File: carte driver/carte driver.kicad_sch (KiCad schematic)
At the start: 38 parts, among them J1 UART CP, J10 STEPPER 4, J11 STEPPER 3, J2 Conn_01x03, J3 UART BONUS, J6 STEPPER G, J7 STEPPER D, J8 STEPPER 1, J9 STEPPER 2, SW2 SW_DIP_x02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

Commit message: c'est l'heure de dodo j'ai bien taffé
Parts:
- added D2: LED_Small, LED_SMD:LED_1206_3216Metric, symbol Device:LED_Small
- added J4: Conn_01x02, Connector_Molex:Molex_KK-254_AE-6410-02A_1x02_P2.54mm_Vertical, symbol Connector_Generic:Conn_01x02
- added R1, R2, R5: 1k, Resistor_SMD:R_1206_3216Metric_Pad1.30x1.75mm_HandSolder, symbol Device:R_Small
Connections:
- net +24V: now also J2.2 (Pin_2); no longer J2.1 (Pin_1)
- net +3.3V: now also J2.1 (Pin_1); no longer U10.12 (VCC_3V3)
- net +5V: now also J4.1 (Pin_1), R5.1; no longer J2.2 (Pin_2)
- net DIR 1: now also U10.4 (GPIO4_D3/A3); no longer U10.2 (GPIO2_D1/A1)
- net DIR 2: now also U10.6 (GPIO6_D5/A5/I2C_SCL); no longer U10.4 (GPIO4_D3/A3)
- net DIR 3: now also U10.2 (GPIO2_D1/A1); no longer U10.6 (GPIO6_D5/A5/I2C_SCL)
- net DIR 5: now also U10.15 (GPIO38_DVP_VSYNC/I2S_SD); no longer U10.16 (GPIO39_CAM_SCL/I2S_SCK)
- net GND: now also D2.1 (K), J4.2 (Pin_2)
- net RX B: now also R1.2; no longer U10.18 (GPIO41_PDM_DATA/RX1)
- net STEP 1: now also U10.3 (GPIO3_D2/A2); no longer U10.1 (GPIO1_D0/A0)
- net STEP 2: now also U10.5 (GPIO5_D4/A4/I2C_SDA); no longer U10.3 (GPIO3_D2/A2)
- net STEP 3: now also U10.1 (GPIO1_D0/A0); no longer U10.5 (GPIO5_D4/A4/I2C_SDA)
- net STEP 5: now also U10.16 (GPIO39_CAM_SCL/I2S_SCK); no longer U10.15 (GPIO38_DVP_VSYNC/I2S_SD)
- net TX B: now also R2.2; no longer U10.19 (GPIO42_PDM_CLK/TX1)
- net at U10.20 (GPIO10_XMCLK/ADC_BAT): now also R2.1
- new net: D2.2 (A), R5.2
- new net: R1.1, U10.19 (GPIO42_PDM_CLK/TX1)
- no-connect marks 30 -> 31

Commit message: apdavph
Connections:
- net at U3.3 (M1B): now also J8.1 (Pin_1); no longer J8.3 (Pin_3)
- net at U3.4 (M1A): now also J8.2 (Pin_2); no longer J8.1 (Pin_1)
- net at U3.5 (M2A): now also J8.3 (Pin_3); no longer J8.2 (Pin_2)
- net at U6.3 (M1B): now also J10.1 (Pin_1); no longer J10.3 (Pin_3)
- net at U6.4 (M1A): now also J10.2 (Pin_2); no longer J10.1 (Pin_1)
- net at U6.5 (M2A): now also J10.3 (Pin_3); no longer J10.2 (Pin_2)
- net at J9.1 (Pin_1): now also U4.3 (M1B); no longer U4.4 (M1A)
- net at J9.2 (Pin_2): now also U4.4 (M1A); no longer U4.5 (M2A)
- net at J9.3 (Pin_3): now also U4.5 (M2A); no longer U4.3 (M1B)
- net at J7.1 (Pin_1): now also U2.3 (M1B); no longer U2.4 (M1A)
- net at J7.2 (Pin_2): now also U2.4 (M1A); no longer U2.5 (M2A)
- net at J7.3 (Pin_3): now also U2.5 (M2A); no longer U2.3 (M1B)
- net at U1.3 (M1B): now also J6.1 (Pin_1); no longer J6.3 (Pin_3)
- net at U1.4 (M1A): now also J6.2 (Pin_2); no longer J6.1 (Pin_1)
- net at U1.5 (M2A): now also J6.3 (Pin_3); no longer J6.2 (Pin_2)
- net at J11.1 (Pin_1): now also U5.3 (M1B); no longer U5.4 (M1A)
- net at J11.2 (Pin_2): now also U5.4 (M1A); no longer U5.5 (M2A)
- net at J11.3 (Pin_3): now also U5.5 (M2A); no longer U5.3 (M1B)
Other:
- moved on the sheet: J10, J11, J6, J7, J8, J9

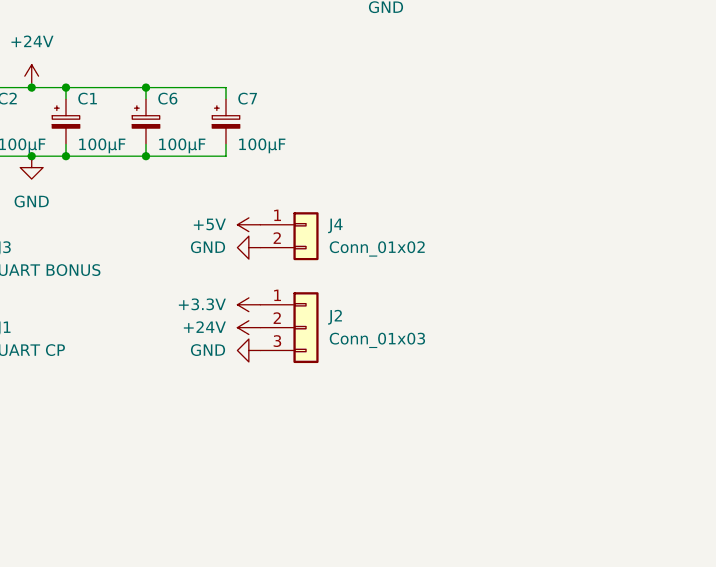
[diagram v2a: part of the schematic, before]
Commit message: changes power input and draw modif
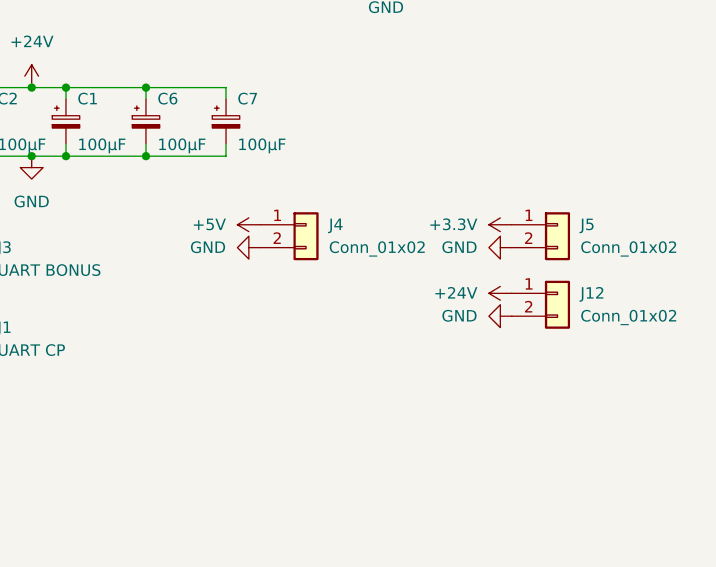
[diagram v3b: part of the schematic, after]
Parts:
- removed J2: Conn_01x03, Connector_JST:JST_EH_B3B-EH-A_1x03_P2.50mm_Vertical, symbol Connector_Generic:Conn_01x03
- added J12: Conn_01x02, Connector_AMASS:AMASS_XT60-F_1x02_P7.20mm_Vertical, symbol Connector_Generic:Conn_01x02
- added J5: Conn_01x02, Connector_AMASS:AMASS_XT30U-F_1x02_P5.0mm_Vertical, symbol Connector_Generic:Conn_01x02
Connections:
- net +24V: now also J12.1 (Pin_1)
- net +3.3V: now also J5.1 (Pin_1)
- net GND: now also J12.2 (Pin_2), J5.2 (Pin_2)
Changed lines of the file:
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@@
 	(symbol
 		(lib_id "power:+3.3V")
-		(at 212.09 151.13 90)
+		(at 240.03 142.24 90)
 		(unit 1)
 		(exclude_from_sim no)
@@
 		(fields_autoplaced yes)
 		(property "Reference" "#PWR015"
-			(at 215.9 151.13 0)
+			(at 243.84 142.24 0)
 			(effects
 				(font
@@
 		)
 		(property "Value" "+3.3V"
-			(at 208.28 151.1299 90)
+			(at 236.22 142.2399 90)
 			(effects
 				(font
@@
 		)
 		(property "Footprint" ""
-			(at 212.09 151.13 0)
+			(at 240.03 142.24 0)
 			(effects
 				(font
@@
 		)
 		(property "Datasheet" ""
-			(at 212.09 151.13 0)
+			(at 240.03 142.24 0)
 			(effects
 				(font
@@
 		)
 		(property "Description" "Power symbol creates a global label with name \"+3.3V\""
-			(at 212.09 151.13 0)
+			(at 240.03 142.24 0)
 			(effects
 				(font
@@
 	(symbol
 		(lib_id "power:GND")
-		(at 212.09 156.21 270)
+		(at 240.03 144.78 270)
 		(unit 1)
 		(exclude_from_sim no)
@@
 		(fields_autoplaced yes)
 		(property "Reference" "#PWR04"
-			(at 205.74 156.21 0)
+			(at 233.68 144.78 0)
 			(effects
 				(font
@@
 		)
 		(property "Value" "GND"
-			(at 208.28 156.2099 90)
+			(at 236.22 144.7799 90)
 			(effects
 				(font
@@
 		)
 		(property "Footprint" ""
-			(at 212.09 156.21 0)
+			(at 240.03 144.78 0)
 			(effects
 				(font
@@
 		)
 		(property "Datasheet" ""
-			(at 212.09 156.21 0)
+			(at 240.03 144.78 0)
 			(effects
 				(font
@@
 		)
 		(property "Description" "Power symbol creates a global label with name \"GND\" , ground"
-			(at 212.09 156.21 0)
+			(at 240.03 144.78 0)
 			(effects
 				(font
@@
 	)
 	(symbol
+		(lib_id "power:GND")
+		(at 240.03 152.4 270)
+		(unit 1)
+		(exclude_from_sim no)
+		(in_bom yes)
+		(on_board yes)
+		(dnp no)
+		(fields_autoplaced yes)
+		(property "Reference" "#PWR08"
+			(at 233.68 152.4 0)
+			(effects
+				(font
+					(size 1.27 1.27)
+				)
+				(hide yes)
+			)
+		)
+		(property "Value" "GND"
+			(at 236.22 152.3999 90)
+			(effects
+				(font
+					(size 1.27 1.27)
+				)
+				(justify right)
+			)
+		)
+		(property "Footprint" ""
+			(at 240.03 152.4 0)
+			(effects
+				(font
+					(size 1.27 1.27)
+				)
+				(hide yes)
+			)
+		)
+		(property "Datasheet" ""
+			(at 240.03 152.4 0)
+			(effects
+				(font
+					(size 1.27 1.27)
+				)
+				(hide yes)
+			)
+		)
+		(property "Description" "Power symbol creates a global label with name \"GND\" , ground"
+			(at 240.03 152.4 0)
+			(effects
+				(font
+					(size 1.27 1.27)
+				)
+				(hide yes)
+			)
+		)
+		(pin "1"
+		)
+		(instances
+			(project "carte driver"
+				(path "/78588076-997a-4987-8ae5-538bbbdafc63"
+					(reference "#PWR08")
+					(unit 1)
+				)
+			)
+		)
+	)
+	(symbol
 		(lib_id "Device:R_Small")
 		(at 140.97 144.78 0)
@@
 	(symbol
 		(lib_id "power:+24V")
-		(at 212.09 153.67 90)
+		(at 240.03 149.86 90)
 		(unit 1)
 		(exclude_from_sim no)
@@
 		(fields_autoplaced yes)
 		(property "Reference" "#PWR01"
-			(at 215.9 153.67 0)
+			(at 243.84 149.86 0)
 			(effects
 				(font
@@
 		)
 		(property "Value" "+24V"
-			(at 208.28 153.6699 90)
+			(at 236.22 149.8599 90)
 			(effects
 				(font
@@
 		)
 		(property "Footprint" ""
-			(at 212.09 153.67 0)
+			(at 240.03 149.86 0)
 			(effects
 				(font
@@
 		)
 		(property "Datasheet" ""
-			(at 212.09 153.67 0)
+			(at 240.03 149.86 0)
 			(effects
 				(font
@@
 		)
 		(property "Description" "Power symbol creates a global label with name \"+24V\""
-			(at 212.09 153.67 0)
+			(at 240.03 149.86 0)
 			(effects
 				(font
@@
 	)
 	(symbol
+		(lib_id "Connector_Generic:Conn_01x02")
+		(at 245.11 149.86 0)
+		(unit 1)
+		(exclude_from_sim no)
+		(in_bom yes)
+		(on_board yes)
+		(dnp no)
+		(fields_autoplaced yes)
+		(property "Reference" "J12"
+			(at 247.65 149.8599 0)
+			(effects
+				(font
+					(size 1.27 1.27)
+				)
+				(justify left)
+			)
+		)
+		(property "Value" "Conn_01x02"
+			(at 247.65 152.3999 0)
+			(effects
+				(font
+					(size 1.27 1.27)
+				)
+				(justify left)
+			)
+		)
+		(property "Footprint" "Connector_AMASS:AMASS_XT60-F_1x02_P7.20mm_Vertical"
+			(at 245.11 149.86 0)
+			(effects
+				(font
+					(size 1.27 1.27)
+				)
+				(hide yes)
+			)
+		)
+		(property "Datasheet" "~"
+			(at 245.11 149.86 0)
+			(effects
+				(font
+					(size 1.27 1.27)
+				)
+				(hide yes)
+			)
+		)
+		(property "Description" "Generic connector, single row, 01x02, script generated (kicad-library-utils/schlib/autogen/connector/)"
+			(at 245.11 149.86 0)
+			(effects
+				(font
+					(size 1.27 1.27)
+				)
+				(hide yes)
+			)
+		)
+		(pin "1"
+		)
+		(pin "2"
+		)
+		(instances
+			(project "carte driver"
+				(path "/78588076-997a-4987-8ae5-538bbbdafc63"
+					(reference "J12")
+					(unit 1)
+				)
+			)
+		)
+	)
+	(symbol
 		(lib_id "Switch:SW_DIP_x02")
 		(at 106.68 48.26 0)
@@
 	)
 	(symbol
+		(lib_id "Connector_Generic:Conn_01x02")
+		(at 245.11 142.24 0)
+		(unit 1)
+		(exclude_from_sim no)
+		(in_bom yes)
+		(on_board yes)
+		(dnp no)
+		(fields_autoplaced yes)
+		(property "Reference" "J5"
+			(at 247.65 142.2399 0)
+			(effects
+				(font
+					(size 1.27 1.27)
+				)
+				(justify left)
+			)
+		)
+		(property "Value" "Conn_01x02"
+			(at 247.65 144.7799 0)
+			(effects
+				(font
+					(size 1.27 1.27)
+				)
+				(justify left)
+			)
+		)
+		(property "Footprint" "Connector_AMASS:AMASS_XT30U-F_1x02_P5.0mm_Vertical"
+			(at 245.11 142.24 0)
+			(effects
+				(font
+					(size 1.27 1.27)
+				)
+				(hide yes)
+			)
+		)
+		(property "Datasheet" "~"
+			(at 245.11 142.24 0)
+			(effects
+				(font
+					(size 1.27 1.27)
+				)
+				(hide yes)
+			)
+		)
+		(property "Description" "Generic connector, single row, 01x02, script generated (kicad-library-utils/schlib/autogen/connector/)"
+			(at 245.11 142.24 0)
+			(effects
+				(font
+					(size 1.27 1.27)
+				)
+				(hide yes)
+			)
+		)
+		(pin "1"
+		)
+		(pin "2"
+		)
+		(instances
+			(project "carte driver"
+				(path "/78588076-997a-4987-8ae5-538bbbdafc63"
+					(reference "J5")
+					(unit 1)
+				)
+			)
+		)
+	)
+	(symbol
 		(lib_id "power:+3.3V")
 		(at 175.26 97.79 0)
@@
 					(unit 1)
 				)
-			)
-		)
-	)
-	(symbol
-		(lib_id "Connector_Generic:Conn_01x03")
-		(at 217.17 153.67 0)
-		(unit 1)
-		(exclude_from_sim no)
-		(in_bom yes)
-		(on_board yes)
-		(dnp no)
-		(fields_autoplaced yes)
-		(property "Reference" "J2"
-			(at 219.71 152.3999 0)
-			(effects
-				(font
-					(size 1.27 1.27)
-				)
-				(justify left)
-			)
-		)
-		(property "Value" "Conn_01x03"
-			(at 219.71 154.9399 0)
-			(effects
-				(font
-					(size 1.27 1.27)
-				)
-				(justify left)
-			)
-		)
-		(property "Footprint" "Connector_JST:JST_EH_B3B-EH-A_1x03_P2.50mm_Vertical"
-			(at 217.17 153.67 0)
-			(effects
-				(font
-					(size 1.27 1.27)
-				)
-				(hide yes)
-			)
-		)
-		(property "Datasheet" "~"
-			(at 217.17 153.67 0)
-			(effects
-				(font
-					(size 1.27 1.27)
-				)
-				(hide yes)
-			)
-		)
-		(property "Description" "Generic connector, single row, 01x03, script generated (kicad-library-utils/schlib/autogen/connector/)"
-			(at 217.17 153.67 0)
-			(effects
-				(font
-					(size 1.27 1.27)
-				)
-				(hide yes)
-			)
-		)
-		(pin "2"
-		)
-		(pin "3"
-		)
-		(pin "1"
-		)
-		(instances
-			(project ""
-				(path "/78588076-997a-4987-8ae5-538bbbdafc63"
-					(reference "J2")
-					(unit 1)
-				)

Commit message: boh il y a des trucs à changé ducoup
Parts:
- J12: value Conn_01x02 -> conn 24v
- J4: value Conn_01x02 -> conn 5v
- J5: value Conn_01x02 -> conn 3.3v
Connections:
- net +24V: now also J12.2 (Pin_2); no longer J12.1 (Pin_1)
- net +3.3V: now also J5.2 (Pin_2); no longer J5.1 (Pin_1)
- net GND: now also J12.1 (Pin_1), J5.1 (Pin_1); no longer J12.2 (Pin_2), J5.2 (Pin_2)
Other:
- moved on the sheet: J12, J4, J5
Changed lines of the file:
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@@
 	(symbol
 		(lib_id "power:+3.3V")
-		(at 240.03 142.24 90)
+		(at 245.11 138.43 90)
 		(unit 1)
 		(exclude_from_sim no)
@@
 		(fields_autoplaced yes)
 		(property "Reference" "#PWR015"
-			(at 243.84 142.24 0)
+			(at 248.92 138.43 0)
 			(effects
 				(font
@@
 		)
 		(property "Value" "+3.3V"
-			(at 236.22 142.2399 90)
+			(at 241.3 138.4299 90)
 			(effects
 				(font
@@
 		)
 		(property "Footprint" ""
-			(at 240.03 142.24 0)
+			(at 245.11 138.43 0)
 			(effects
 				(font
@@
 		)
 		(property "Datasheet" ""
-			(at 240.03 142.24 0)
+			(at 245.11 138.43 0)
 			(effects
 				(font
@@
 		)
 		(property "Description" "Power symbol creates a global label with name \"+3.3V\""
-			(at 240.03 142.24 0)
+			(at 245.11 138.43 0)
 			(effects
 				(font
@@
 		)
 		(instances
-			(project ""
+			(project "carte driver"
 				(path "/78588076-997a-4987-8ae5-538bbbdafc63"
 					(reference "#PWR015")
@@
 	(symbol
 		(lib_id "power:GND")
-		(at 240.03 144.78 270)
+		(at 245.11 135.89 270)
 		(unit 1)
 		(exclude_from_sim no)
@@
 		(fields_autoplaced yes)
 		(property "Reference" "#PWR04"
-			(at 233.68 144.78 0)
+			(at 238.76 135.89 0)
 			(effects
 				(font
@@
 		)
 		(property "Value" "GND"
-			(at 236.22 144.7799 90)
+			(at 241.3 135.8899 90)
 			(effects
 				(font
@@
 		)
 		(property "Footprint" ""
-			(at 240.03 144.78 0)
+			(at 245.11 135.89 0)
 			(effects
 				(font
@@
 		)
 		(property "Datasheet" ""
-			(at 240.03 144.78 0)
+			(at 245.11 135.89 0)
 			(effects
 				(font
@@
 		)
 		(property "Description" "Power symbol creates a global label with name \"GND\" , ground"
-			(at 240.03 144.78 0)
+			(at 245.11 135.89 0)
 			(effects
 				(font
@@
 		)
 		(instances
-			(project ""
+			(project "carte driver"
 				(path "/78588076-997a-4987-8ae5-538bbbdafc63"
 					(reference "#PWR04")
@@
 	(symbol
 		(lib_id "power:GND")
-		(at 212.09 144.78 270)
+		(at 245.11 144.78 270)
 		(unit 1)
 		(exclude_from_sim no)
@@
 		(fields_autoplaced yes)
 		(property "Reference" "#PWR016"
-			(at 205.74 144.78 0)
+			(at 238.76 144.78 0)
 			(effects
 				(font
@@
 		)
 		(property "Value" "GND"
-			(at 208.28 144.7799 90)
+			(at 241.3 144.7799 90)
 			(effects
 				(font
@@
 		)
 		(property "Footprint" ""
-			(at 212.09 144.78 0)
+			(at 245.11 144.78 0)
 			(effects
 				(font
@@
 		)
 		(property "Datasheet" ""
-			(at 212.09 144.78 0)
+			(at 245.11 144.78 0)
 			(effects
 				(font
@@
 		)
 		(property "Description" "Power symbol creates a global label with name \"GND\" , ground"
-			(at 212.09 144.78 0)
+			(at 245.11 144.78 0)
 			(effects
 				(font
@@
 	(symbol
 		(lib_id "power:GND")
-		(at 240.03 152.4 270)
+		(at 245.11 148.59 270)
 		(unit 1)
 		(exclude_from_sim no)
@@
 		(fields_autoplaced yes)
 		(property "Reference" "#PWR08"
-			(at 233.68 152.4 0)
+			(at 238.76 148.59 0)
 			(effects
 				(font
@@
 		)
 		(property "Value" "GND"
-			(at 236.22 152.3999 90)
+			(at 241.3 148.5899 90)
 			(effects
 				(font
@@
 		)
 		(property "Footprint" ""
-			(at 240.03 152.4 0)
+			(at 245.11 148.59 0)
 			(effects
 				(font
@@
 		)
 		(property "Datasheet" ""
-			(at 240.03 152.4 0)
+			(at 245.11 148.59 0)
 			(effects
 				(font
@@
 		)
 		(property "Description" "Power symbol creates a global label with name \"GND\" , ground"
-			(at 240.03 152.4 0)
+			(at 245.11 148.59 0)
 			(effects
 				(font
@@
 	(symbol
 		(lib_id "power:+24V")
-		(at 240.03 149.86 90)
+		(at 245.11 151.13 90)
 		(unit 1)
 		(exclude_from_sim no)
@@
 		(fields_autoplaced yes)
 		(property "Reference" "#PWR01"
-			(at 243.84 149.86 0)
+			(at 248.92 151.13 0)
 			(effects
 				(font
@@
 		)
 		(property "Value" "+24V"
-			(at 236.22 149.8599 90)
+			(at 241.3 151.1299 90)
 			(effects
 				(font
@@
 		)
 		(property "Footprint" ""
-			(at 240.03 149.86 0)
+			(at 245.11 151.13 0)
 			(effects
 				(font
@@
 		)
 		(property "Datasheet" ""
-			(at 240.03 149.86 0)
+			(at 245.11 151.13 0)
 			(effects
 				(font
@@
 		)
 		(property "Description" "Power symbol creates a global label with name \"+24V\""
-			(at 240.03 149.86 0)
+			(at 245.11 151.13 0)
 			(effects
 				(font
@@
 	(symbol
 		(lib_id "Connector_Generic:Conn_01x02")
-		(at 217.17 142.24 0)
+		(at 250.19 142.24 0)
 		(unit 1)
 		(exclude_from_sim no)
@@
 		(fields_autoplaced yes)
 		(property "Reference" "J4"
-			(at 219.71 142.2399 0)
+			(at 252.73 142.2399 0)
 			(effects
 				(font
@@
 			)
 		)
-		(property "Value" "Conn_01x02"
-			(at 219.71 144.7799 0)
+		(property "Value" "conn 5v"
+			(at 252.73 144.7799 0)
 			(effects
 				(font
@@
 		)
 		(property "Footprint" "Connector_Molex:Molex_KK-254_AE-6410-02A_1x02_P2.54mm_Vertical"
-			(at 217.17 142.24 0)
+			(at 250.19 142.24 0)
 			(effects
 				(font
@@
 		)
 		(property "Datasheet" "~"
-			(at 217.17 142.24 0)
+			(at 250.19 142.24 0)
 			(effects
 				(font
@@
 		)
 		(property "Description" "Generic connector, single row, 01x02, script generated (kicad-library-utils/schlib/autogen/connector/)"
-			(at 217.17 142.24 0)
+			(at 250.19 142.24 0)
 			(effects
 				(font
@@
 	(symbol
 		(lib_id "Connector_Generic:Conn_01x02")
-		(at 245.11 149.86 0)
+		(at 250.19 148.59 0)
 		(unit 1)
 		(exclude_from_sim no)
@@
 		(fields_autoplaced yes)
 		(property "Reference" "J12"
-			(at 247.65 149.8599 0)
+			(at 252.73 148.5899 0)
 			(effects
 				(font
@@
 			)
 		)
-		(property "Value" "Conn_01x02"
-			(at 247.65 152.3999 0)
+		(property "Value" "conn 24v"
+			(at 252.73 151.1299 0)
 			(effects
 				(font
@@
 		)
 		(property "Footprint" "Connector_AMASS:AMASS_XT60-F_1x02_P7.20mm_Vertical"
-			(at 245.11 149.86 0)
+			(at 250.19 148.59 0)
 			(effects
 				(font
@@
 		)
 		(property "Datasheet" "~"
-			(at 245.11 149.86 0)
+			(at 250.19 148.59 0)
 			(effects
 				(font
@@
 		)
 		(property "Description" "Generic connector, single row, 01x02, script generated (kicad-library-utils/schlib/autogen/connector/)"
-			(at 245.11 149.86 0)
+			(at 250.19 148.59 0)
 			(effects
 				(font
@@
 	(symbol
 		(lib_id "power:+5V")
-		(at 212.09 142.24 90)
+		(at 245.11 142.24 90)
 		(unit 1)
 		(exclude_from_sim no)
@@
 		(fields_autoplaced yes)
 		(property "Reference" "#PWR02"
-			(at 215.9 142.24 0)
+			(at 248.92 142.24 0)
 			(effects
 				(font
@@
 		)
 		(property "Value" "+5V"
-			(at 208.28 142.2399 90)
+			(at 241.3 142.2399 90)
 			(effects
 				(font
@@
 		)
 		(property "Footprint" ""
-			(at 212.09 142.24 0)
+			(at 245.11 142.24 0)
 			(effects
 				(font
@@
 		)
 		(property "Datasheet" ""
-			(at 212.09 142.24 0)
+			(at 245.11 142.24 0)
 			(effects
 				(font
@@
 		)
 		(property "Description" "Power symbol creates a global label with name \"+5V\""
-			(at 212.09 142.24 0)
+			(at 245.11 142.24 0)
 			(effects
 				(font
@@
 	(symbol
 		(lib_id "Connector_Generic:Conn_01x02")
-		(at 245.11 142.24 0)
+		(at 250.19 135.89 0)
 		(unit 1)
 		(exclude_from_sim no)
@@
 		(fields_autoplaced yes)
 		(property "Reference" "J5"
-			(at 247.65 142.2399 0)
+			(at 252.73 135.8899 0)
 			(effects
 				(font
@@
 			)
 		)
-		(property "Value" "Conn_01x02"
-			(at 247.65 144.7799 0)
+		(property "Value" "conn 3.3v"
+			(at 252.73 138.4299 0)
 			(effects
 				(font
@@
 		)
 		(property "Footprint" "Connector_AMASS:AMASS_XT30U-F_1x02_P5.0mm_Vertical"
-			(at 245.11 142.24 0)
+			(at 250.19 135.89 0)
 			(effects
 				(font
@@
 		)
 		(property "Datasheet" "~"
-			(at 245.11 142.24 0)
+			(at 250.19 135.89 0)
 			(effects
 				(font
@@
 		)
 		(property "Description" "Generic connector, single row, 01x02, script generated (kicad-library-utils/schlib/autogen/connector/)"
-			(at 245.11 142.24 0)
+			(at 250.19 135.89 0)
 			(effects
 				(font
